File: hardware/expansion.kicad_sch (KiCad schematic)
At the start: 8 parts, among them J1 EXP, J2 EXP, J3 EXP, J4 EXP, J5 EXP, J6 EXP, J7 EXP, J8 EXP

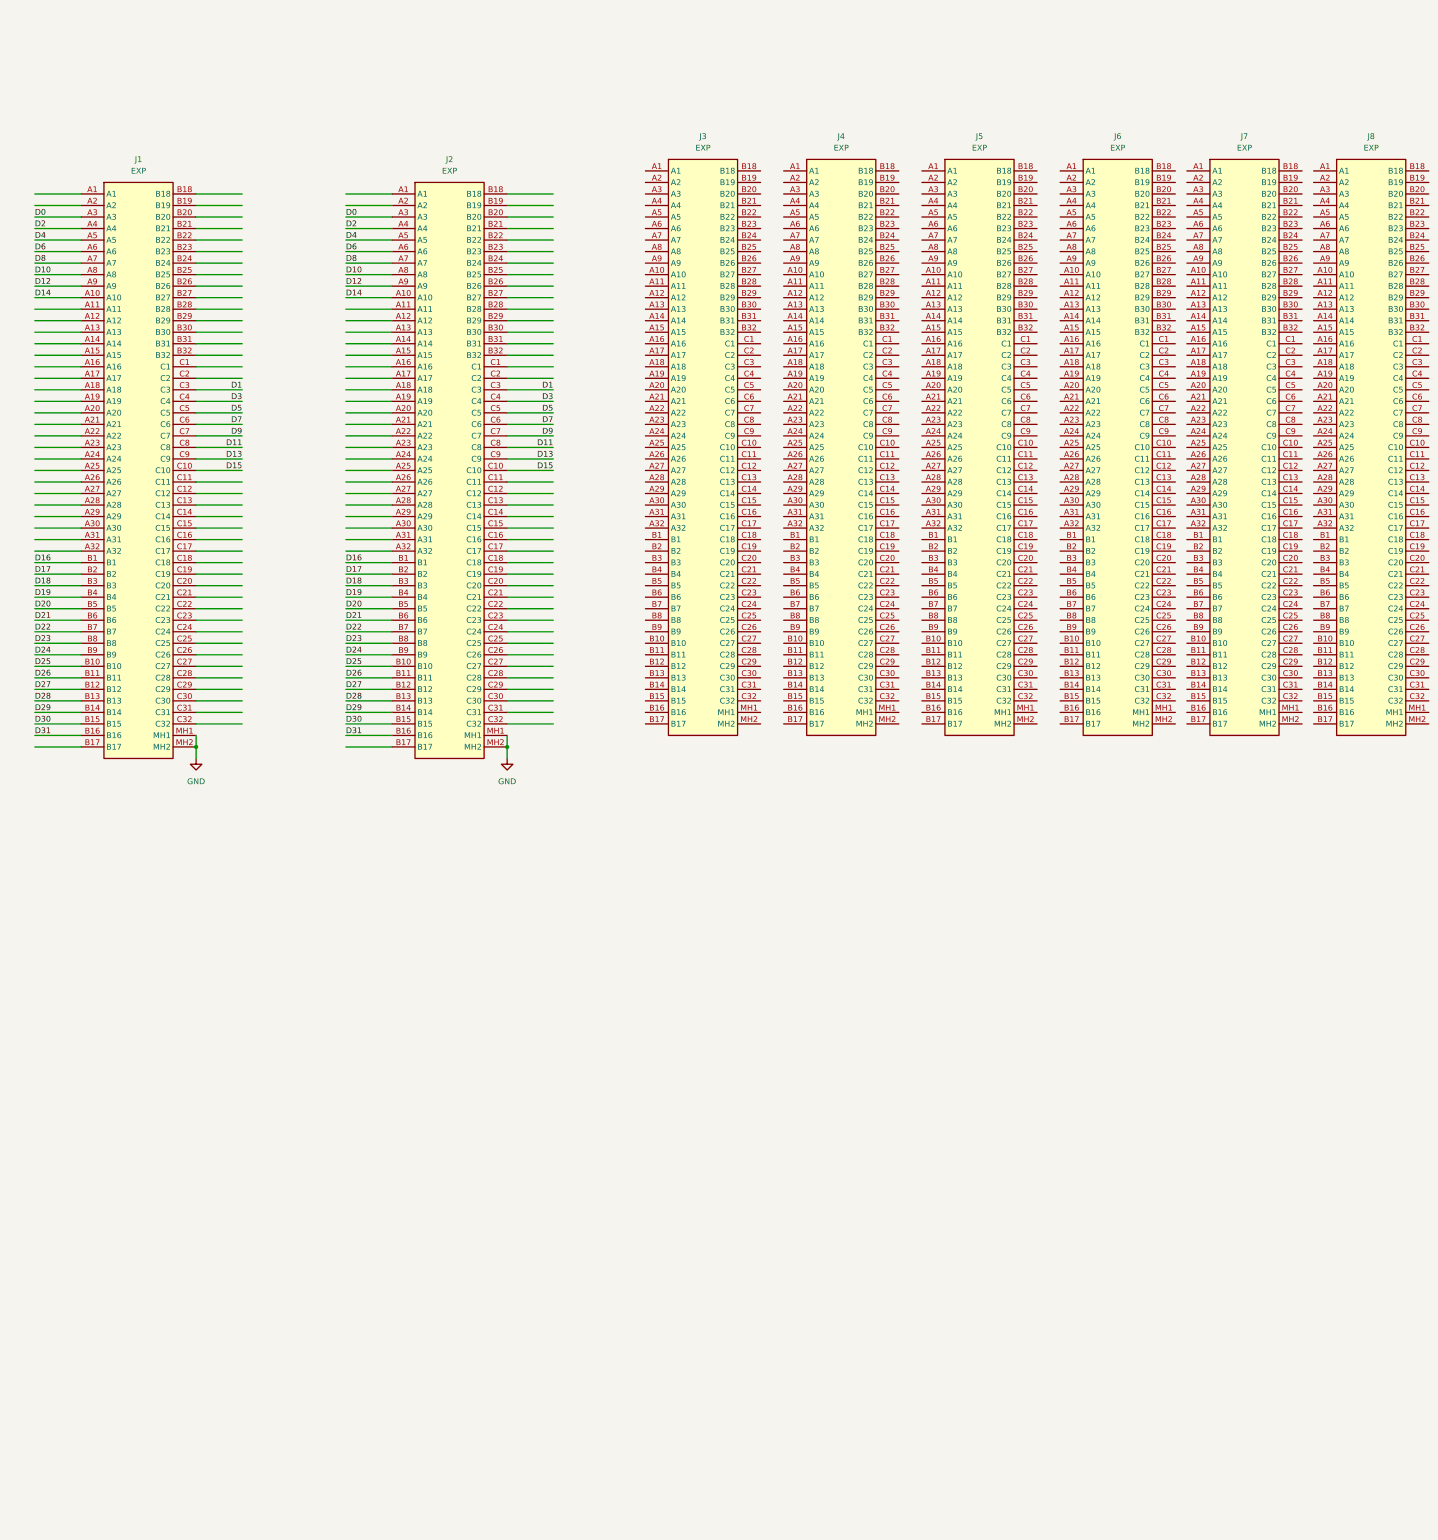
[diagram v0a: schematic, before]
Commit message: reformat expanison port symbol
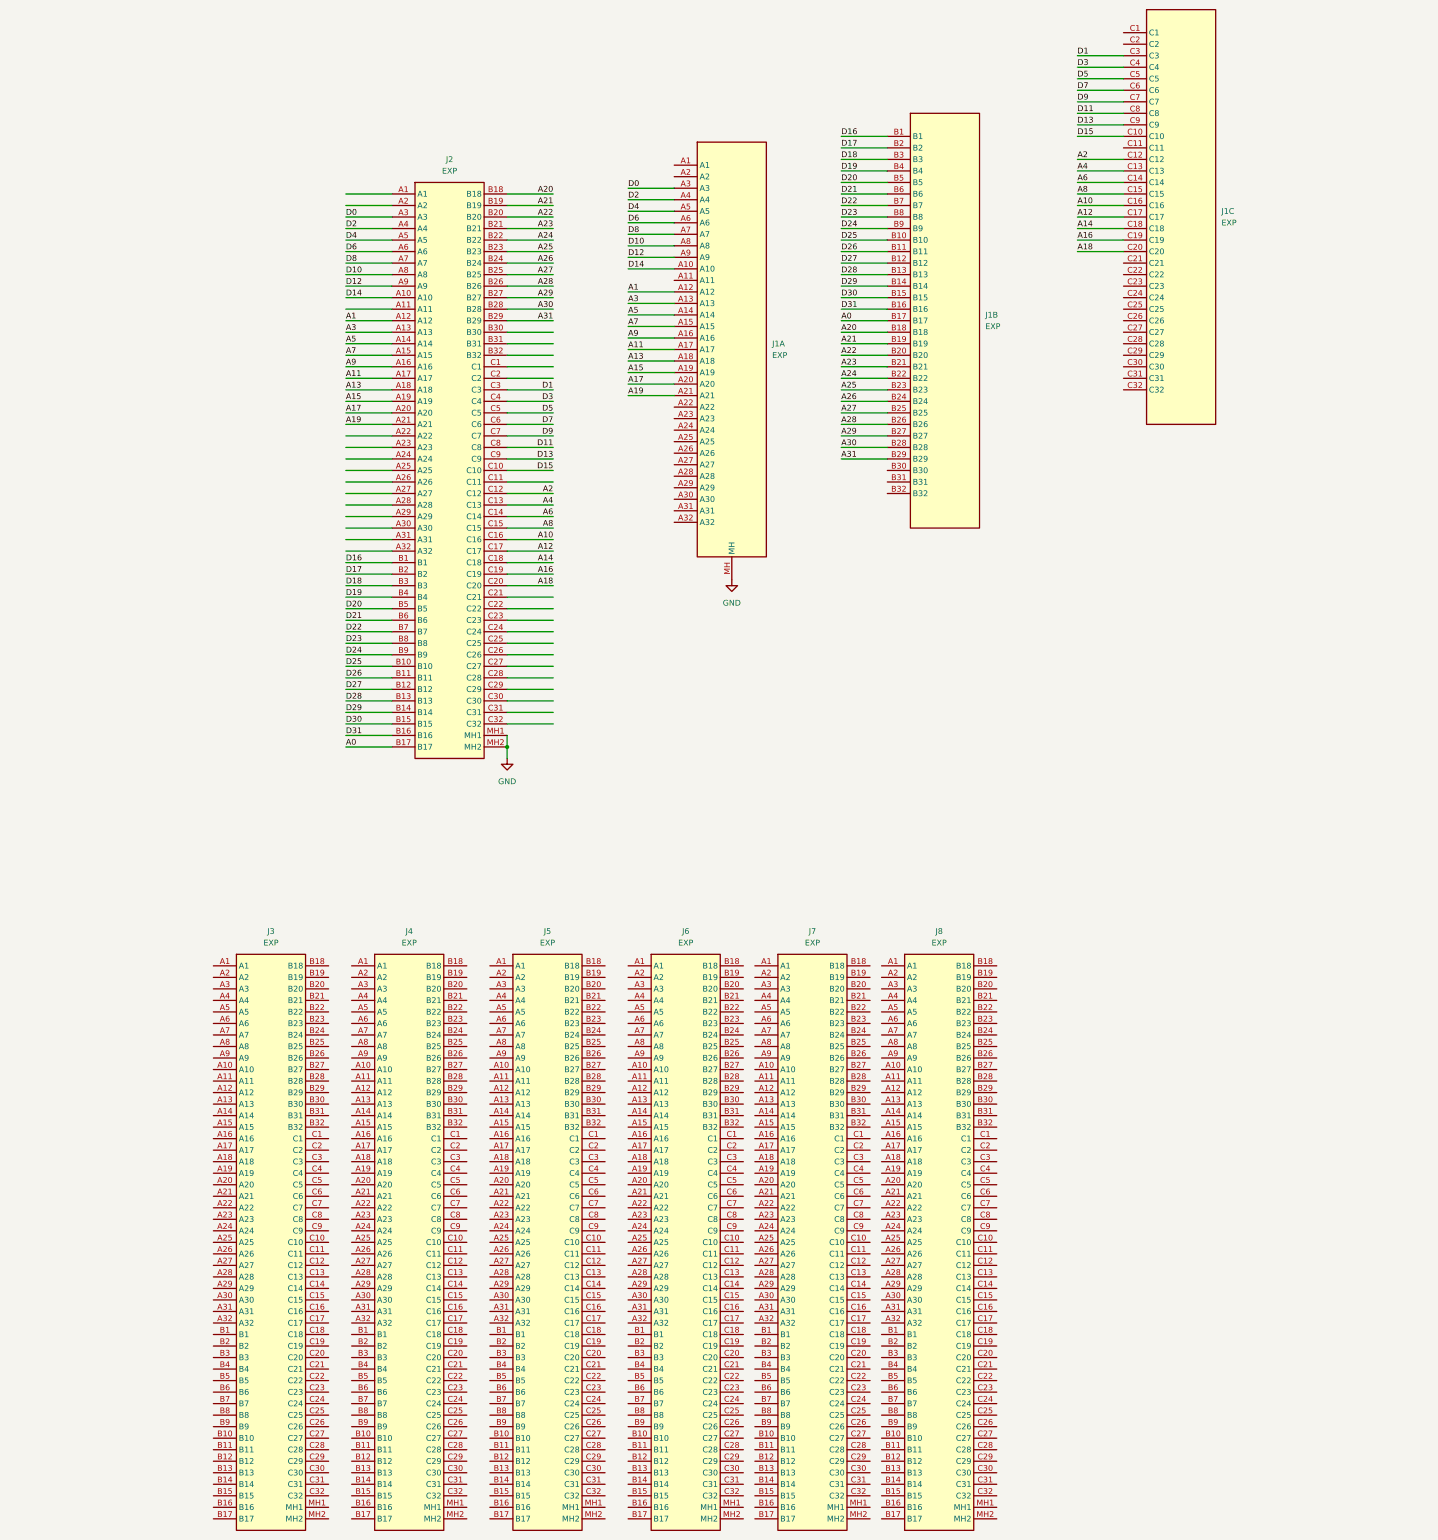
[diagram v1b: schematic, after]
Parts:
- added unit 3 of J1
- added unit 2 of J1
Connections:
- net D1: now also J1.C3; no longer J1.C3
- net D11: now also J1.C8; no longer J1.C8
- net D13: now also J1.C9; no longer J1.C9
- net D15: now also J1.C10; no longer J1.C10
- net D16: now also J1.B1; no longer J1.B1
- net D17: now also J1.B2; no longer J1.B2
- net D18: now also J1.B3; no longer J1.B3
- net D19: now also J1.B4; no longer J1.B4
- net D20: now also J1.B5; no longer J1.B5
- net D21: now also J1.B6; no longer J1.B6
- net D22: now also J1.B7; no longer J1.B7
- net D23: now also J1.B8; no longer J1.B8
- net D24: now also J1.B9; no longer J1.B9
- net D25: now also J1.B10; no longer J1.B10
- net D26: now also J1.B11; no longer J1.B11
- net D27: now also J1.B12; no longer J1.B12
- net D28: now also J1.B13; no longer J1.B13
- net D29: now also J1.B14; no longer J1.B14
- net D3: now also J1.C4; no longer J1.C4
- net D30: now also J1.B15; no longer J1.B15
- net D31: now also J1.B16; no longer J1.B16
- net D5: now also J1.C5; no longer J1.C5
- net D7: now also J1.C6; no longer J1.C6
- net D9: now also J1.C7; no longer J1.C7
- net GND: now also J1.MH; no longer J1.MH1, J1.MH2
- net A1: now reaches J2.A12
- net A1: now also J1.A12
- net A3: now reaches J2.A13
- net A3: now also J1.A13
- net A5: now reaches J2.A14
- net A5: now also J1.A14
- net A7: now reaches J2.A15
- net A7: now also J1.A15
- net A9: now reaches J2.A16
- net A9: now also J1.A16
- net A11: now reaches J2.A17
- net A11: now also J1.A17
- net A13: now reaches J2.A18
- net A13: now also J1.A18
- net A15: now reaches J2.A19
- net A15: now also J1.A19
- net A17: now reaches J2.A20
- net A17: now also J1.A20
- net A19: now reaches J2.A21
- net A19: now also J1.A21
- net A0: now reaches J2.B17
- net A0: now also J1.B17
- net A20: now reaches J2.B18
- net A20: now also J1.B18
- net A21: now reaches J2.B19
- net A21: now also J1.B19
- net A22: now reaches J2.B20
- net A22: now also J1.B20
- net A23: now reaches J2.B21
- net A23: now also J1.B21
- net A24: now reaches J2.B22
- net A24: now also J1.B22
- net A25: now reaches J2.B23
- net A25: now also J1.B23
- net A26: now reaches J2.B24
- net A26: now also J1.B24
- net A27: now reaches J2.B25
- net A27: now also J1.B25
- net A28: now reaches J2.B26
- net A28: now also J1.B26
- net A29: now reaches J2.B27
- net A29: now also J1.B27
- net A30: now reaches J2.B28
- net A30: now also J1.B28
- net A31: now reaches J2.B29
- net A31: now also J1.B29
- net A2: now reaches J2.C12
- net A2: now also J1.C12
- net A4: now reaches J2.C13
- net A4: now also J1.C13
- net A6: now reaches J2.C14
- net A6: now also J1.C14
- net A8: now reaches J2.C15
- net A8: now also J1.C15
- net A10: now reaches J2.C16
- net A10: now also J1.C16
- net A12: now reaches J2.C17
- net A12: now also J1.C17
- net A14: now reaches J2.C18
- net A14: now also J1.C18
- net A16: now reaches J2.C19
- net A16: now also J1.C19
- net A18: now reaches J2.C20
- net A18: now also J1.C20
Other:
- moved on the sheet: J3, J4, J5, J6, J7, J8

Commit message: reconfigure expansion slot schematic
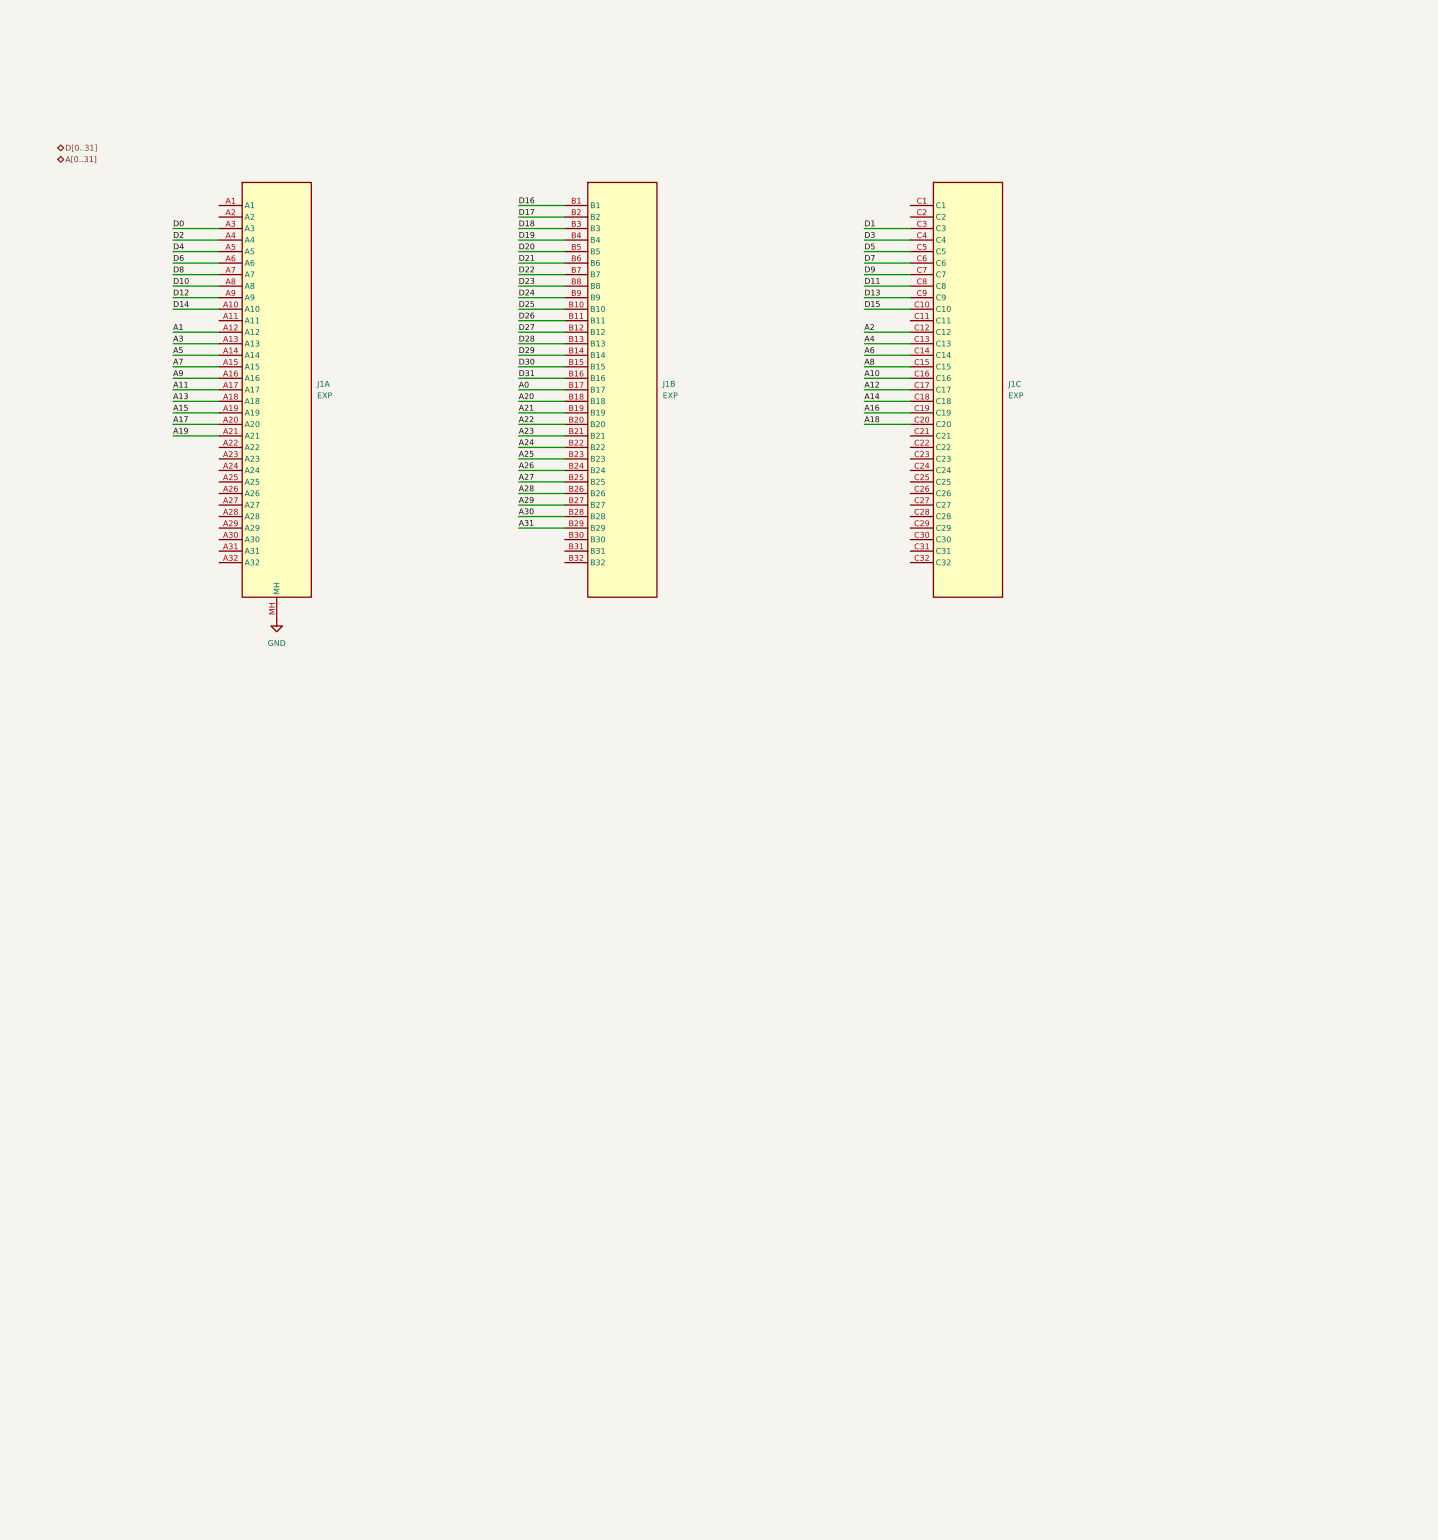
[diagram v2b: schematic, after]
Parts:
- removed J2, J3, J4, J5, J6, J7, J8: EXP, 68040:EXP, symbol 68040:EXP
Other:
- moved on the sheet: J1A, J1B, J1C

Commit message: updates
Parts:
- renumbered J1 to J2
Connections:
- net GND: now also J2.A1, J2.A11, J2.A32, J2.B32, J2.C11, J2.C24, J2.C32
- net +5V: now reaches J2.C1
- net +5V: now also J2.A24
- net ~{CFG_{OUT}}: now reaches J2.C2
- net +3V3: now reaches J2.C30
- net +12V: now reaches J2.C31
- net +12V: now also J2.A31
- net ~{CFG_{IN}}: now reaches J2.A2
- net BCLK: now reaches J2.B31
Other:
- note added: "1 2 3 4 5 6 7 8 9 10 11 12 13 14 15 16 17"

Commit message: updates
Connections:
- net A0 renamed EXA0
- net A1 renamed EXA1
- net A10 renamed EXA10
- net A11 renamed EXA11
- net A12 renamed EXA12
- net A13 renamed EXA13
- net A14 renamed EXA14
- net A15 renamed EXA15
- net A16 renamed EXA16
- net A17 renamed EXA17
- net A18 renamed EXA18
- net A19 renamed EXA19
- net A2 renamed EXA2
- net A20 renamed EXA20
- net A21 renamed EXA21
- net A22 renamed EXA22
- net A23 renamed EXA23
- net A24 renamed EXA24
- net A25 renamed EXA25
- net A26 renamed EXA26
- net A27 renamed EXA27
- net A28 renamed EXA28
- net A29 renamed EXA29
- net A3 renamed EXA3
- net A30 renamed EXA30
- net A31 renamed EXA31
- net A4 renamed EXA4
- net A5 renamed EXA5
- net A6 renamed EXA6
- net A7 renamed EXA7
- net A8 renamed EXA8
- net A9 renamed EXA9
- net D0 renamed EXD0
- net D1 renamed EXD1
- net D10 renamed EXD10
- net D11 renamed EXD11
- net D12 renamed EXD12
- net D13 renamed EXD13
- net D14 renamed EXD14
- net D15 renamed EXD15
- net D16 renamed EXD16
- net D17 renamed EXD17
- net D18 renamed EXD18
- net D19 renamed EXD19
- net D2 renamed EXD2
- net D20 renamed EXD20
- net D21 renamed EXD21
- net D22 renamed EXD22
- net D23 renamed EXD23
- net D24 renamed EXD24
- net D25 renamed EXD25
- net D26 renamed EXD26
- net D27 renamed EXD27
- net D28 renamed EXD28
- net D29 renamed EXD29
- net D3 renamed EXD3
- net D30 renamed EXD30
- net D31 renamed EXD31
- net D4 renamed EXD4
- net D5 renamed EXD5
- net D6 renamed EXD6
- net D7 renamed EXD7
- net D8 renamed EXD8
- net D9 renamed EXD9

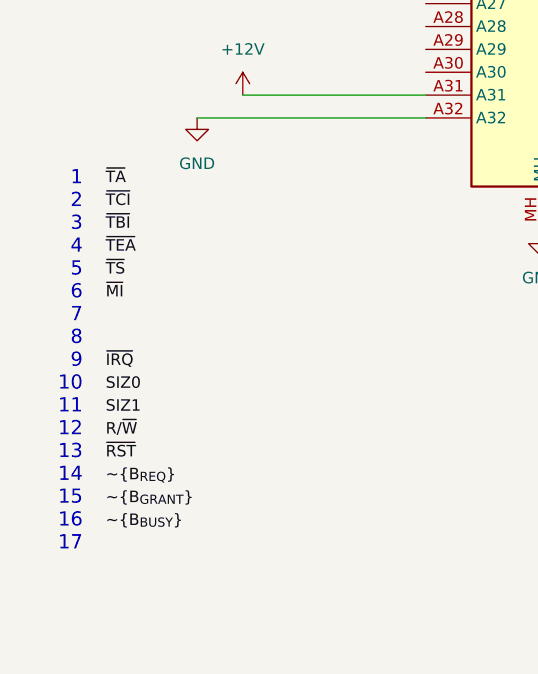
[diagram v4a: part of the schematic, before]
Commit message: begin work on a simpler first draft board
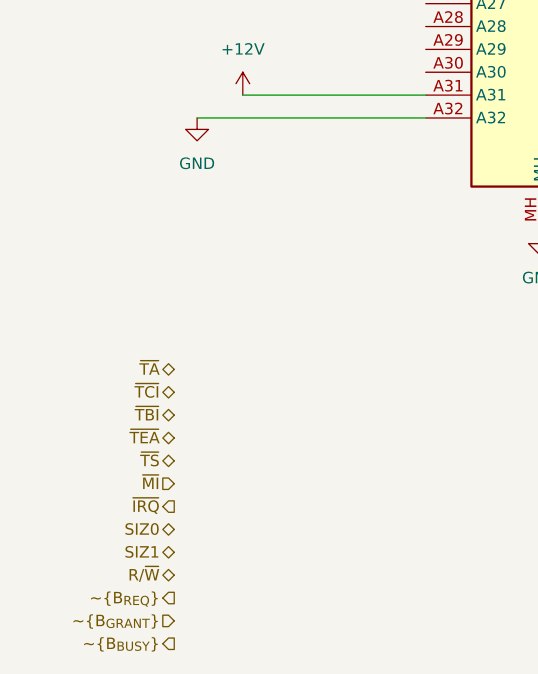
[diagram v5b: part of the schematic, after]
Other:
- note removed: "1 2 3 4 5 6 7 8 9 10 11 12 13 14 15 16 17"
